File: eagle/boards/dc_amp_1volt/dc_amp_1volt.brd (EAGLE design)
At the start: 100 x 80 mm, 11 parts, among them U1 LM358

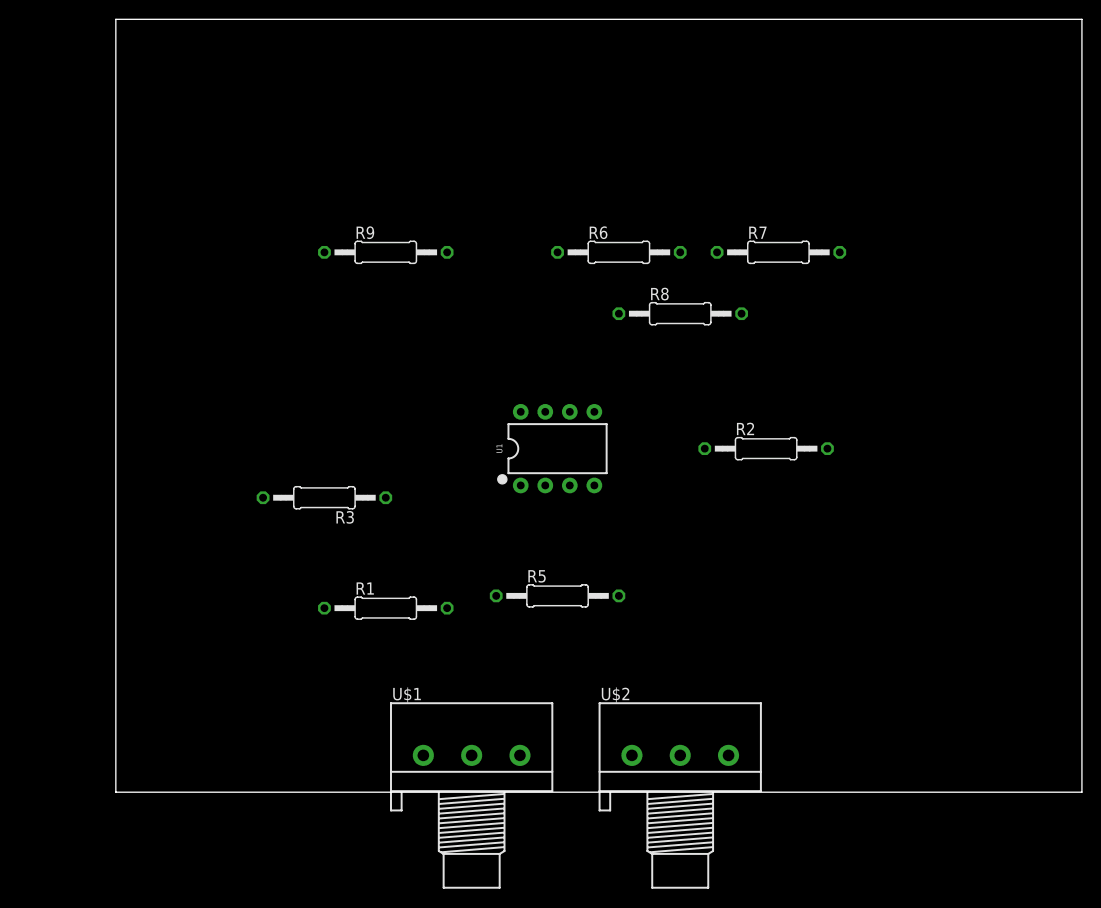
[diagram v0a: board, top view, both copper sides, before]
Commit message: DC coupled Amp with limiter + board
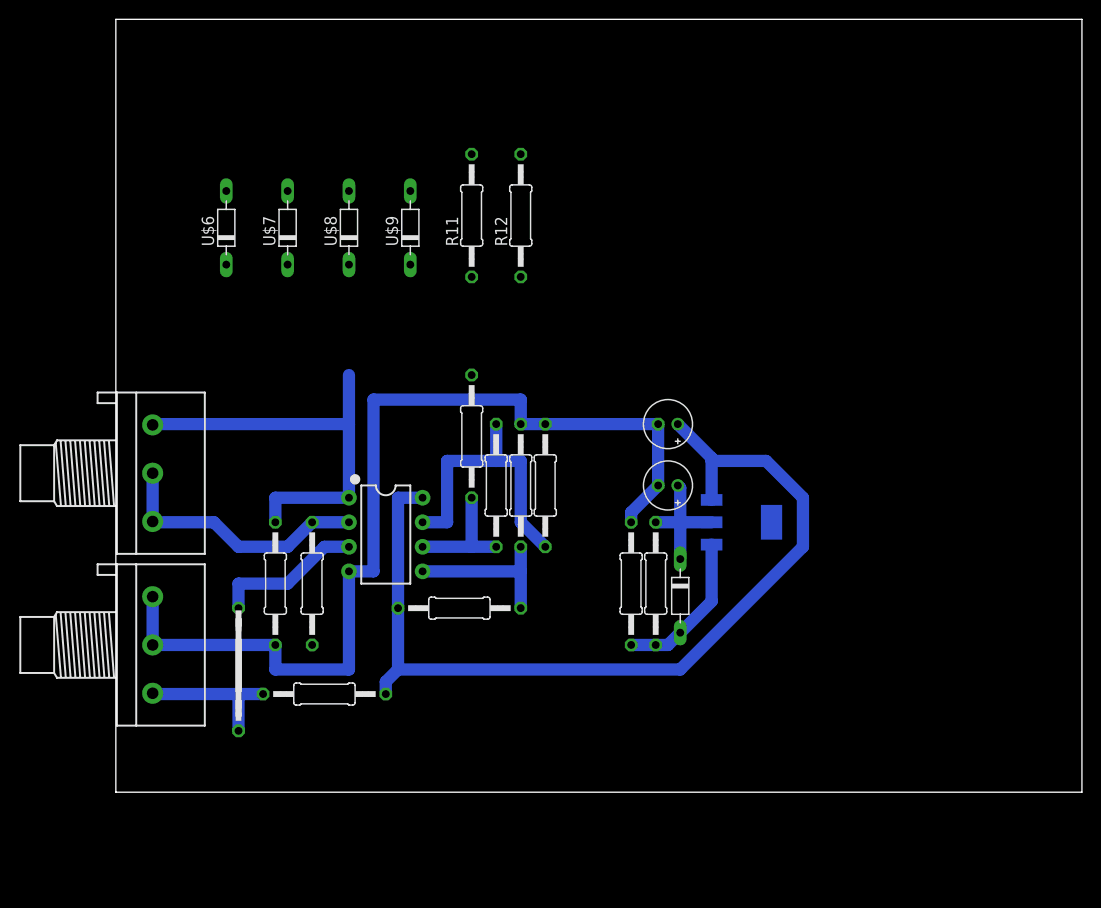
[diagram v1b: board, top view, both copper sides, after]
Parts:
- added C1: 10u, adq_proc_components:E2-5
- added C2: 22u, adq_proc_components:E2-5
- added R10: 115, adq_proc_components:0207/12
- added R11, R12: 5k, adq_proc_components:0207/12
- added R4: 220, adq_proc_components:0207/12
- added U$3: NCP1117, adq_proc_components:SOT223
- added U$4, U$6, U$7, U$8, U$9: 1N4148, adq_proc_components:D-7.5
- added U$5: BRIDGE, adq_proc_components:BRIDGE
- moved U$2 55.8 mm to (3.81, 15.2), turned to 270 degrees
- moved U$1 44.1 mm to (3.81, 33.0), turned to 270 degrees
- moved R7 37.9 mm to (39.4, 31.8), turned to 90 degrees
- moved R9 37.6 mm to (35.6, 19.1), turned to 180 degrees
- moved R5 26.2 mm to (21.6, 10.2), turned to 180 degrees
- moved R6 24.4 mm to (36.8, 36.8), turned to 270 degrees
- moved R8 24.3 mm to (41.9, 31.8), turned to 270 degrees
- moved R2 23.2 mm to (44.5, 31.8), turned to 270 degrees
- moved U1 19.9 mm to (27.9, 26.7), turned to 270 degrees
- moved R3 10.2 mm to (16.5, 21.6), turned to 90 degrees
- moved R1 8.03 mm to (20.3, 21.6), turned to 90 degrees
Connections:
- removed net DC_L: R5.1, R9.2, U1.8
- new net DC5_L: C1.+, R5.1, R9.2, U$3.3, U1.8
- new net DC_ADJ_L: C2.+, R11.2, R4.2, U$3.2, U$4.C
- new net N$11: R6.1, U$7.C, U$9.A
- new net N$4: R12.1, U$8.C, U$9.C
- new net N$6: R10.2, R4.1, U$3.1, U$4.A
- new net N$7: R11.1, U$6.A, U$7.A
- net 0: now also C1.-, C2.-, R10.1, R12.2
- net N$1: now also U$5.1, U$5.2
- net VOUT_1: now also U$6.C, U$8.A; no longer R6.1
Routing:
- net 0: track 0.00 -> 101.7 mm
- net DC5_L: track 0.00 -> 96.0 mm
- net VOUT_1: track 0.00 -> 43.2 mm
- net N$1: track 0.00 -> 30.8 mm
- net OUT: track 0.00 -> 30.3 mm
- net N$3: track 0.00 -> 27.5 mm
- net N$2: track 0.00 -> 16.5 mm
- net N$6: track 0.00 -> 16.1 mm
- net DC_ADJ_L: track 0.00 -> 13.5 mm
- net N$5: track 0.00 -> 12.7 mm

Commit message: DC Amp. presets added
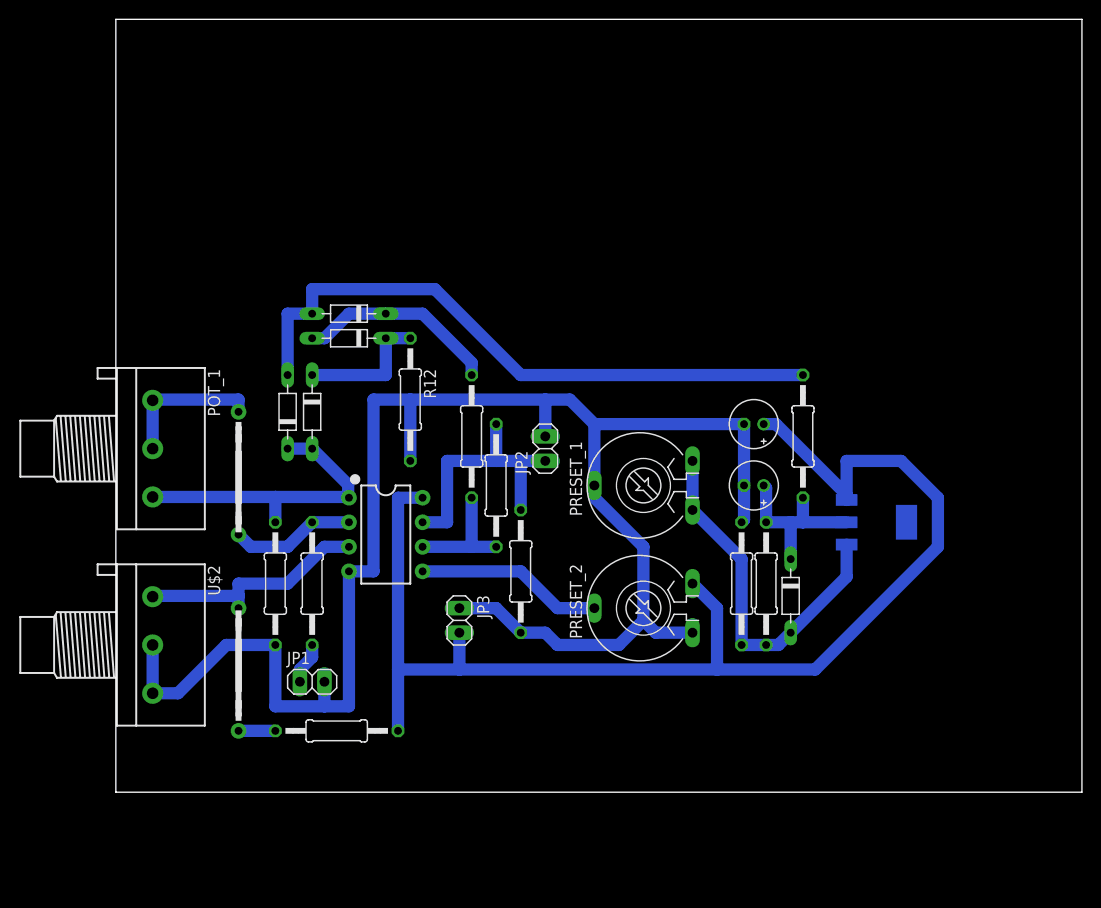
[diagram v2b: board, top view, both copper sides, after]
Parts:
- removed R8: 10k, adq_proc_components:0207/12
- removed R9: 14k, adq_proc_components:0207/12
- added JP1, JP2, JP3: (no value), pinhead:1X02
- added POT_1: POT_1, adq_proc:3RP/1610N
- added PRESET_1, PRESET_2: PRESET-10MM, adq_proc:PT-10
- R10: value 115 -> 330
- U$1: value POT_A -> BRIDGE; device adq_proc_components:3RP/1610N -> adq_proc:BRIDGE
- U$2: value POT_B -> POT_2; device adq_proc_components:3RP/1610N -> adq_proc:3RP/1610N
- U$5: device adq_proc_components:BRIDGE -> adq_proc:BRIDGE
- moved R11 41.2 mm to (71.1, 36.8), turned to 270 degrees
- moved R12 22.2 mm to (30.5, 40.6), turned to 270 degrees
- moved U$1 22.2 mm to (12.7, 12.7)
- moved U$5 20.3 mm to (12.7, 33.0), turned to 90 degrees
- moved U$6 20.1 mm to (17.8, 39.4)
- moved U$8 19.4 mm to (20.3, 39.4), turned to 270 degrees
- moved U$3 14.0 mm to (78.7, 27.9)
- moved U$9 13.1 mm to (24.1, 47.0), turned to 180 degrees
- moved R4 11.4 mm to (67.3, 21.6)
- moved R10 11.4 mm to (64.8, 21.6)
- moved U$4 11.4 mm to (69.8, 20.3)
- moved U$7 10.9 mm to (24.1, 49.5), turned to 180 degrees
- moved R2 9.25 mm to (41.9, 22.9), turned to 90 degrees
- moved C1 8.89 mm to (66.0, 38.1)
- moved C2 8.89 mm to (66.0, 31.8)
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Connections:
- removed net N$6: R10.2, R4.1, U$3.1, U$4.A
- new net N$8: PRESET_1.A, PRESET_1.E, R10.2, R4.1, U$3.1, U$4.A
- net 0: now also JP1.2, JP2.2, JP3.1, PRESET_1.S, PRESET_2.A, U$2.3; no longer R8.1, U$2.1
- net DC5_L: now also JP3.2, PRESET_2.E; no longer R9.2
- net IN_L: now also JP1.1
- net N$1: now also U$1.1, U$1.2, U$2.1; no longer U$2.3, U$5.1, U$5.2
- net N$2: now also PRESET_2.S; no longer R8.2, R9.1
- net N$3: now also POT_1.1, POT_1.2, U$5.1, U$5.2; no longer U$1.2, U$1.3
- net OUT: now also JP2.1
- net VOUT_1: now also POT_1.3; no longer U$1.1
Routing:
- net 0: track 101.7 -> 180.1 mm
- net N$7: track 0.00 -> 65.9 mm
- net N$8: track 0.00 -> 38.3 mm
- net DC5_L: track 96.0 -> 133.9 mm
- net N$11: track 0.00 -> 20.9 mm
- net N$6: track 16.1 -> 0.00 mm
- net N$4: track 0.00 -> 14.0 mm
- net VOUT_1: track 43.2 -> 32.1 mm
- net DC_ADJ_L: track 13.5 -> 18.6 mm
- net IN_L: track 0.00 -> 4.34 mm
- net N$2: track 16.5 -> 19.4 mm
- net N$1: track 30.8 -> 28.3 mm
- net OUT: track 30.3 -> 27.9 mm
- net N$3: track 27.5 -> 28.2 mm
